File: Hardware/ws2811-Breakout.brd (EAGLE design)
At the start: 17.8 x 12.7 mm, 9 parts, among them U1 LED-TRICOLOR-5050

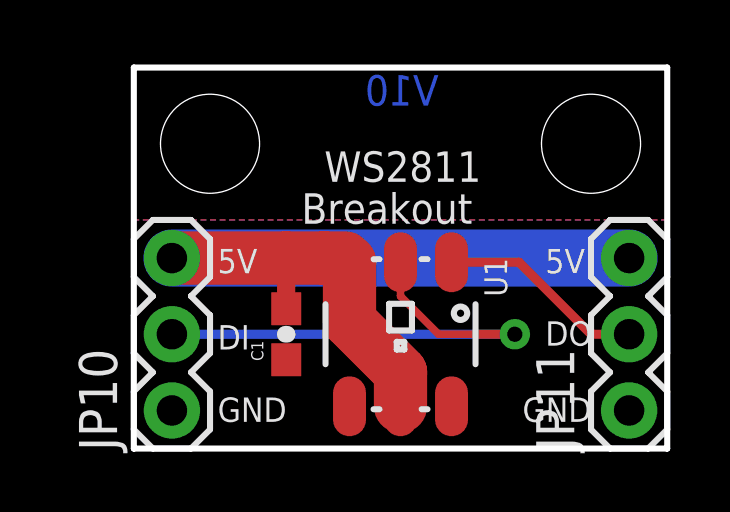
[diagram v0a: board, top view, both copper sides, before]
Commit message: v10 Ready for production
Organized files/folders
Added fiducial marks to design
Created panel array of boards for manufacture
v12 now tagged as v10 (initial production ready design)
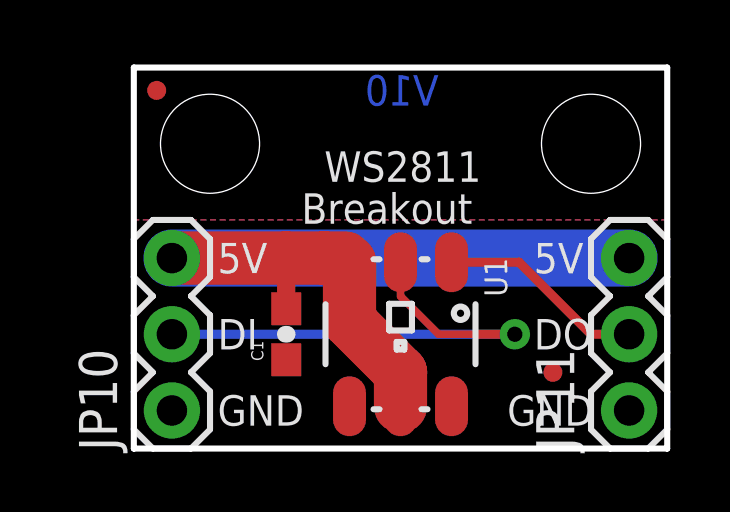
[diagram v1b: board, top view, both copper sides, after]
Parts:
- removed FRAME2: FRAME-LETTER, SparkFun-Aesthetics:CREATIVE_COMMONS
- added FID1, FID2: FIDUCIALUFIDUCIAL, SparkFun-Aesthetics:MICRO-FIDUCIAL
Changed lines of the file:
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@@
 <setting verticaltext="up"/>
 </settings>
-<grid distance="0.05" unitdist="inch" unit="inch" style="lines" multiple="1" display="yes" altdistance="0.005" altunitdist="inch" altunit="inch"/>
+<grid distance="0.05" unitdist="inch" unit="inch" style="lines" multiple="1" display="yes" altdistance="0.01" altunitdist="inch" altunit="inch"/>
 <layers>
 <layer number="1" name="Top" color="4" fill="1" visible="yes" active="yes"/>
@@
 <layer number="18" name="Vias" color="2" fill="1" visible="yes" active="yes"/>
 <layer number="19" name="Unrouted" color="6" fill="1" visible="yes" active="yes"/>
-<layer number="20" name="Dimension" color="7" fill="1" visible="yes" active="yes"/>
-<layer number="21" name="tPlace" color="16" fill="1" visible="yes" active="yes"/>
-<layer number="22" name="bPlace" color="14" fill="1" visible="yes" active="yes"/>
+<layer number="20" name="Dimension" color="6" fill="1" visible="yes" active="yes"/>
+<layer number="21" name="tPlace" color="6" fill="1" visible="yes" active="yes"/>
+<layer number="22" name="bPlace" color="6" fill="1" visible="yes" active="yes"/>
 <layer number="23" name="tOrigins" color="15" fill="1" visible="yes" active="yes"/>
 <layer number="24" name="bOrigins" color="15" fill="1" visible="yes" active="yes"/>
@@
 <layer number="47" name="Measures" color="7" fill="1" visible="no" active="yes"/>
 <layer number="48" name="Document" color="7" fill="1" visible="no" active="yes"/>
-<layer number="49" name="Reference" color="7" fill="1" visible="yes" active="yes"/>
+<layer number="49" name="Reference" color="7" fill="1" visible="no" active="yes"/>
 <layer number="50" name="dxf" color="7" fill="1" visible="no" active="yes"/>
 <layer number="51" name="tDocu" color="6" fill="1" visible="yes" active="yes"/>
@@
 <wire x1="17.78" y1="12.7" x2="17.78" y2="0" width="0.2032" layer="20"/>
 <wire x1="17.78" y1="0" x2="0" y2="0" width="0.2032" layer="20"/>
-<text x="13.716" y="5.842" size="0.8128" layer="21" font="vector" ratio="15">5V</text>
-<text x="2.794" y="3.302" size="0.8128" layer="21" font="vector" ratio="15">DI</text>
-<text x="12.954" y="0.889" size="0.8128" layer="21" font="vector" ratio="15">GND</text>
-<text x="2.794" y="5.842" size="0.8128" layer="21" font="vector" ratio="15">5V</text>
-<text x="13.716" y="3.429" size="0.8128" layer="21" font="vector" ratio="15">DO</text>
-<text x="2.794" y="0.889" size="0.8128" layer="21" font="vector" ratio="15">GND</text>
+<text x="13.335" y="5.842" size="1.016" layer="21" font="vector" ratio="15">5V</text>
+<text x="2.794" y="3.302" size="1.016" layer="21" font="vector" ratio="15">DI</text>
+<text x="12.446" y="0.762" size="1.016" layer="21" font="vector" ratio="15">GND</text>
+<text x="2.794" y="5.842" size="1.016" layer="21" font="vector" ratio="15">5V</text>
+<text x="13.335" y="3.302" size="1.016" layer="21" font="vector" ratio="15">DO</text>
+<text x="2.794" y="0.762" size="1.016" layer="21" font="vector" ratio="15">GND</text>
 <text x="10.16" y="11.43" size="1.016" layer="16" ratio="20" rot="MR0">V10</text>
 <text x="4.572" y="5.842" size="1.016" layer="22" font="vector" ratio="15" rot="MR0">5V</text>
@@
 <element name="JP11" library="SparkFun-Connectors" package="1X03" value="OUTPUT" x="16.51" y="1.27" rot="R90"/>
 <element name="LOGO1" library="SparkFun-Aesthetics" package="OSHW-LOGO-S" value="OSHW-LOGOS" x="6.35" y="3.81" rot="MR0"/>
-<element name="FRAME2" library="SparkFun-Aesthetics" package="CREATIVE_COMMONS" value="FRAME-LETTER" x="-13.97" y="-17.78"/>
+<element name="FID1" library="SparkFun-Aesthetics" package="MICRO-FIDUCIAL" value="FIDUCIALUFIDUCIAL" x="0.762" y="11.938"/>
+<element name="FID2" library="SparkFun-Aesthetics" package="MICRO-FIDUCIAL" value="FIDUCIALUFIDUCIAL" x="13.97" y="2.54"/>
 </elements>
 <signals>
